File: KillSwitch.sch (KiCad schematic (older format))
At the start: 21 parts, among them J0 Screw_Terminal_1x04, J1 CONN_01X04, J2 CONN_01X04, J3 CONN_01X02, J4 CONN_01X04, Q0 IRF1324PBF, Q1 IRF1324PBF, Q2 IRF1324PBF, Q3 IRF1324PBF, U0 NC7SZ08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

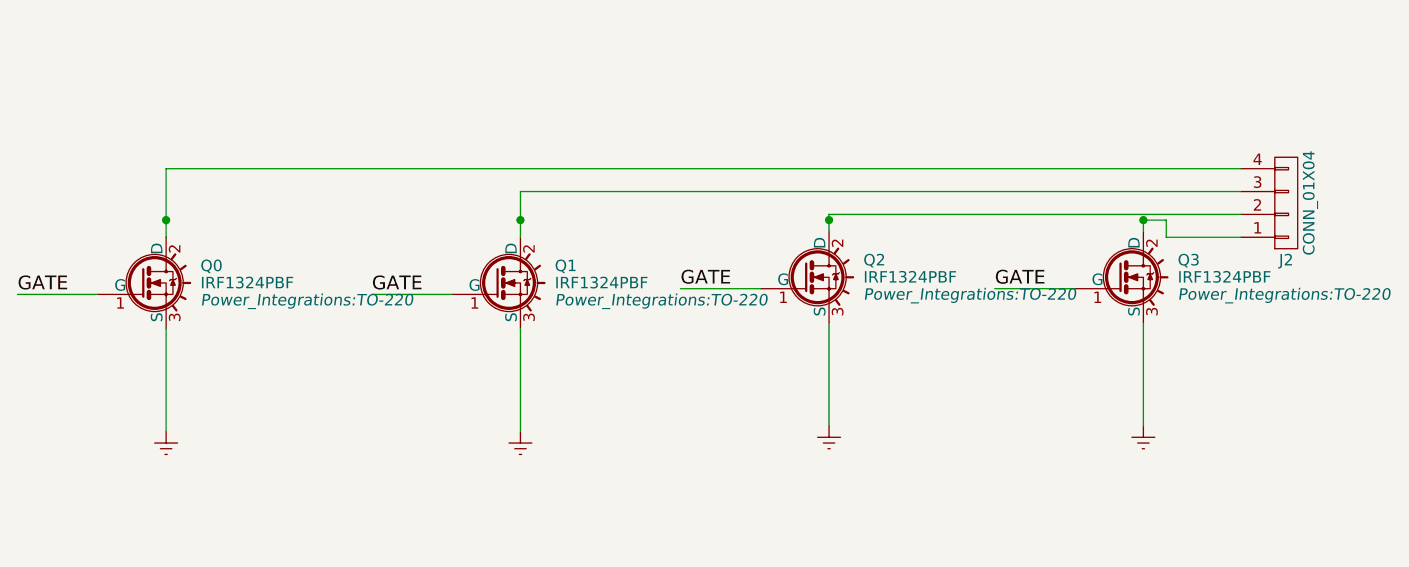
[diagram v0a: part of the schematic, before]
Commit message: Add varistors to DS
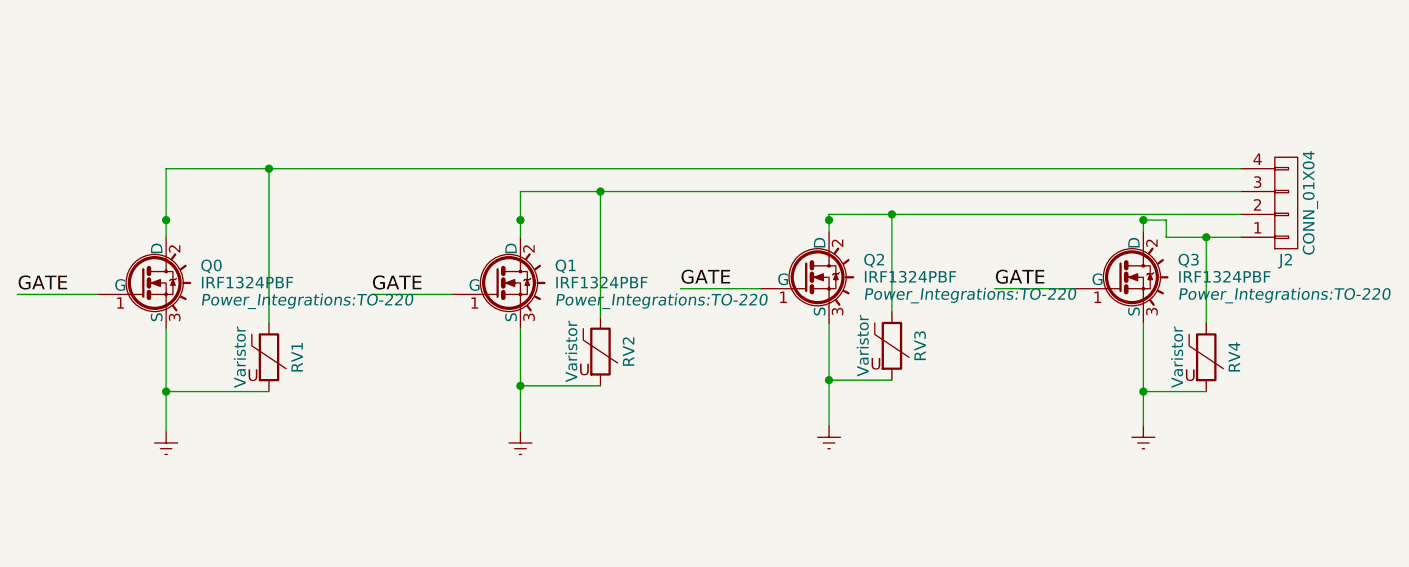
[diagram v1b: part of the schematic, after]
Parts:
- added RV1, RV2, RV3, RV4: Varistor, Resistors_SMD:R_1210_HandSoldering, symbol Varistor
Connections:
- net Earth: now also RV1.2, RV2.2, RV3.2, RV4.2
- net at J2.3 (P3), Q1.2 (D): now also RV2.1
- net at J2.1 (P1), Q3.2 (D): now also RV4.1
- net at J2.4 (P4), Q0.2 (D): now also RV1.1
- net at J2.2 (P2), Q2.2 (D): now also RV3.1
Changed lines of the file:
@@
 Wire Wire Line
 	6575 2250 6575 1950
+$Comp
+L Varistor RV1
+U 1 1 5935DAD7
+P 6200 5850
+F 0 "RV1" V 6325 5850 50  0000 C CNN
+F 1 "Varistor" V 6075 5850 50  0000 C CNN
+F 2 "Resistors_SMD:R_1210_HandSoldering" V 6130 5850 50  0001 C CNN
+F 3 "" H 6200 5850 50  0001 C CNN
+	1    6200 5850
+	1    0    0    -1
+$EndComp
+Wire Wire Line
+	6200 5700 6200 5025
+Connection ~ 6200 5025
+Wire Wire Line
+	6200 6000 5750 6000
+Connection ~ 5750 6000
+$Comp
+L Varistor RV2
+U 1 1 5935DDCC
+P 7650 5825
+F 0 "RV2" V 7775 5825 50  0000 C CNN
+F 1 "Varistor" V 7525 5825 50  0000 C CNN
+F 2 "Resistors_SMD:R_1210_HandSoldering" V 7580 5825 50  0001 C CNN
+F 3 "" H 7650 5825 50  0001 C CNN
+	1    7650 5825
+	1    0    0    -1
+$EndComp
+$Comp
+L Varistor RV3
+U 1 1 5935DE45
+P 8925 5800
+F 0 "RV3" V 9050 5800 50  0000 C CNN
+F 1 "Varistor" V 8800 5800 50  0000 C CNN
+F 2 "Resistors_SMD:R_1210_HandSoldering" V 8855 5800 50  0001 C CNN
+F 3 "" H 8925 5800 50  0001 C CNN
+	1    8925 5800
+	1    0    0    -1
+$EndComp
+$Comp
+L Varistor RV4
+U 1 1 5935DEB7
+P 10300 5850
+F 0 "RV4" V 10425 5850 50  0000 C CNN
+F 1 "Varistor" V 10175 5850 50  0000 C CNN
+F 2 "Resistors_SMD:R_1210_HandSoldering" V 10230 5850 50  0001 C CNN
+F 3 "" H 10300 5850 50  0001 C CNN
+	1    10300 5850
+	1    0    0    -1
+$EndComp
+Wire Wire Line
+	10300 5325 10300 5700
+Connection ~ 10300 5325
+Wire Wire Line
+	10300 6000 10025 6000
+Connection ~ 10025 6000
+Wire Wire Line
+	8925 5650 8925 5225
+Connection ~ 8925 5225
+Wire Wire Line
+	8925 5950 8650 5950
+Connection ~ 8650 5950
+Wire Wire Line
+	7650 5675 7650 5125
+Connection ~ 7650 5125
+Wire Wire Line
+	7650 5975 7300 5975
+Connection ~ 7300 5975
 $EndSCHEMATC
